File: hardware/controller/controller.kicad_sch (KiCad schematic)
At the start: 2 parts, among them U3 Baochip, U4 Baochip

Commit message: remove wrong part from controller board
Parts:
- removed U3, U4: Baochip, common:Dabao_Vendor_Substrate, symbol common:Dabao

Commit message: more controller board work
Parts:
- added U5, U6, U7, U8: ZX-PM2.54-1-16PY, easyeda2kicad:HDR-TH_16P-P2.54-V-F-1, symbol easyeda2kicad:ZX-PM2.54-1-16PY

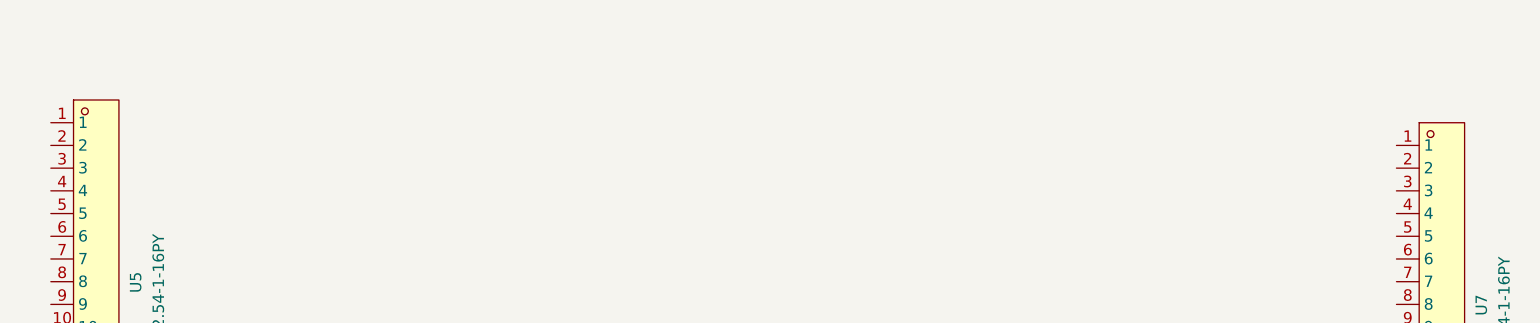
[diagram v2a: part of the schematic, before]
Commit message: adding labels and the barrel connector
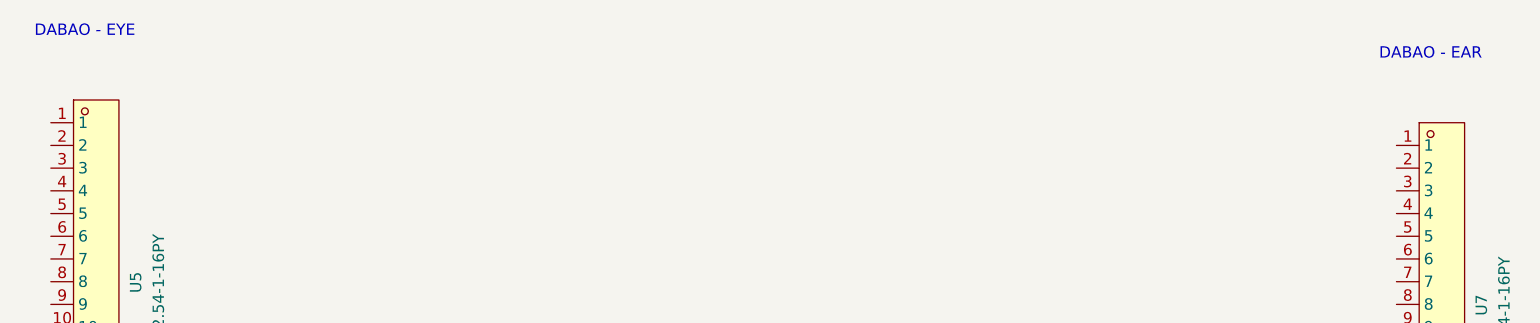
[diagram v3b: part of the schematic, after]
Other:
- note added: "DABAO - EAR"
- note added: "DABAO - EYE"
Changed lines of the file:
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@@
 	(generator_version "10.0")
 	(paper "A4")
+	(text "DABAO - EYE"
+		(exclude_from_sim no)
+		(at 97.79 27.94 0)
+		(effects
+			(font
+				(size 1.27 1.27)
+			)
+		)
+	)
+	(text "DABAO - EAR"
+		(exclude_from_sim no)
+		(at 248.285 30.48 0)
+		(effects
+			(font
+				(size 1.27 1.27)
+			)
+		)
+	)
 	(symbol
 		(lib_id "easyeda2kicad:ZX-PM2.54-1-16PY")

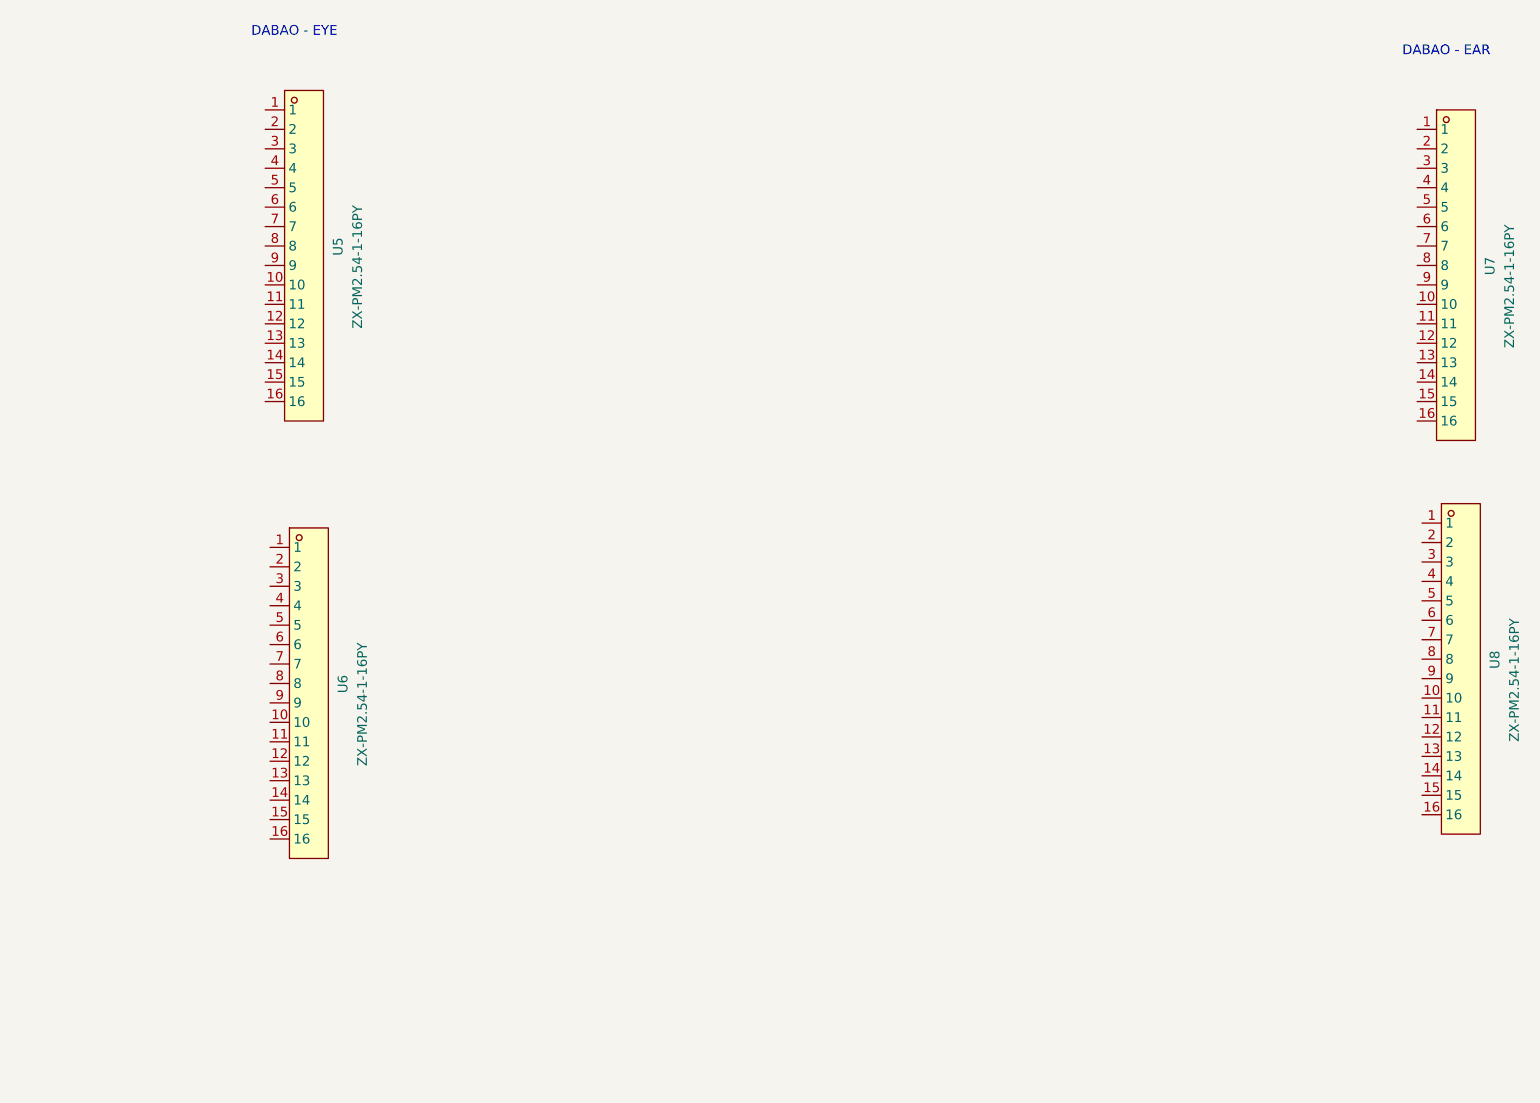
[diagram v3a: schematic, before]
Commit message: hook up all the dabao headers and one more voltage converter
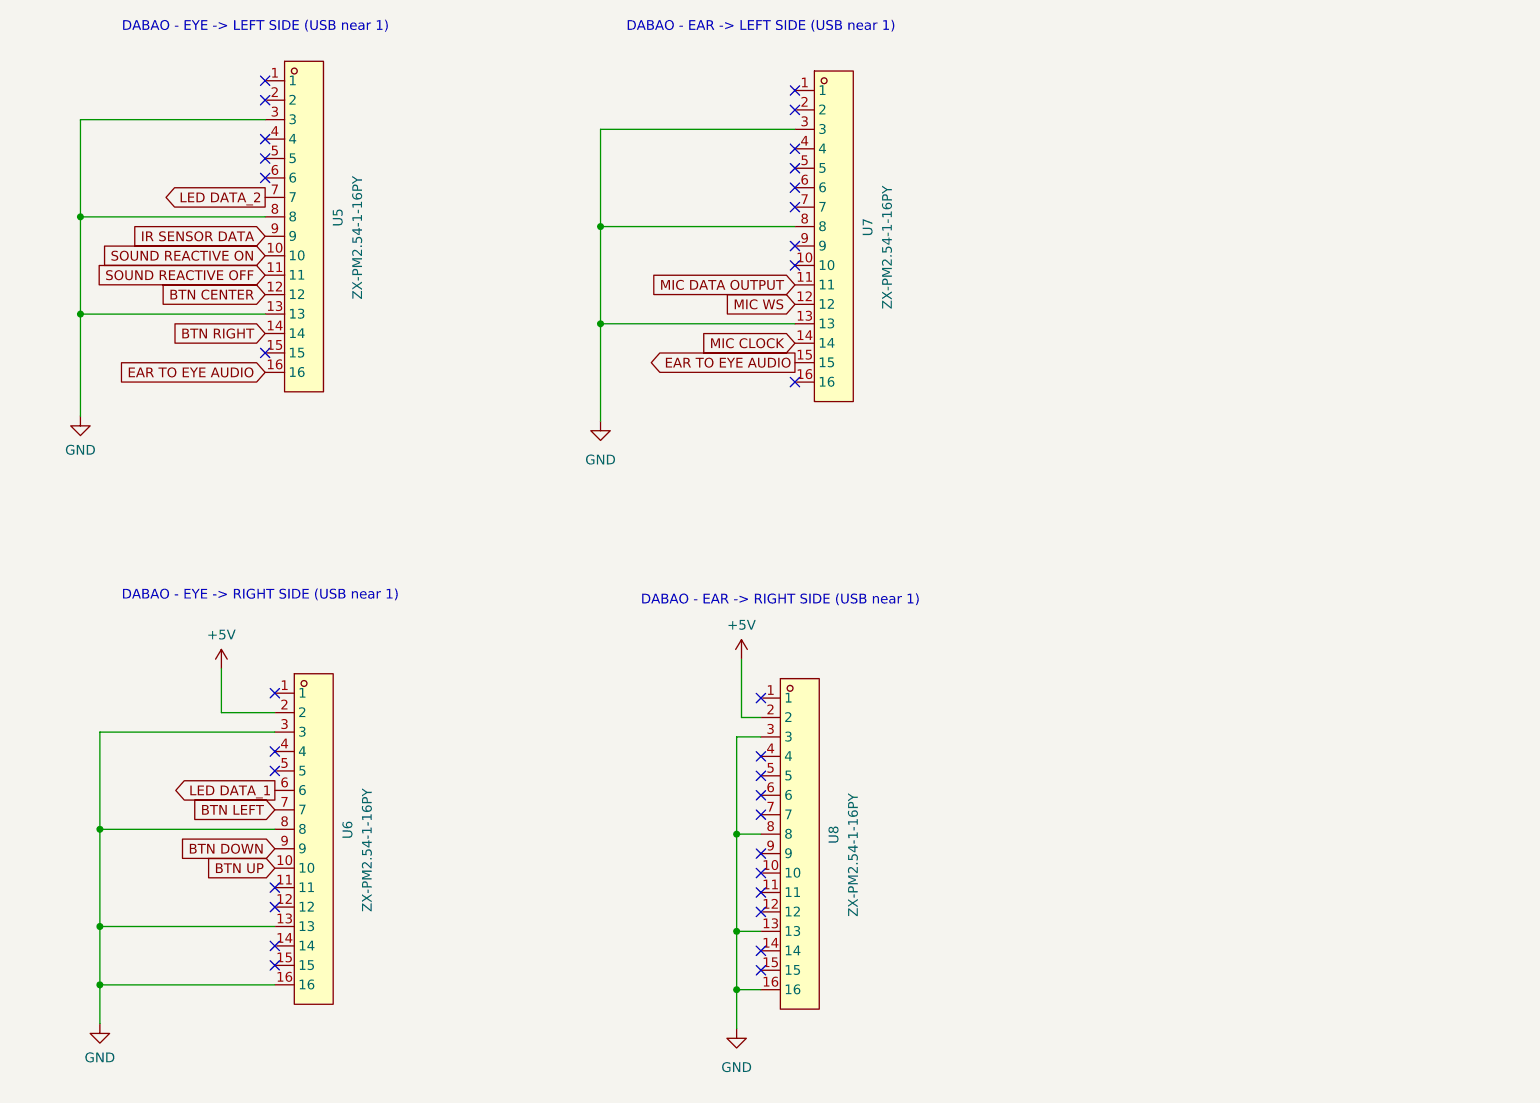
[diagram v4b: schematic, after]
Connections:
- net BTN UP: now reaches U6.10
- net GND: now reaches U6.13
- net GND: now also U5.13, U5.3, U5.8, U6.16, U6.3, U6.8, U7.13, U7.3, U7.8, U8.13, U8.16, U8.3, U8.8
- net +5V: now reaches U6.2
- net +5V: now also U8.2
- net LED DATA_1: now reaches U6.6
- net BTN LEFT: now reaches U6.7
- net BTN DOWN: now reaches U6.9
- net SOUND REACTIVE ON: now reaches U5.10
- net SOUND REACTIVE OFF: now reaches U5.11
- net BTN CENTER: now reaches U5.12
- net BTN RIGHT: now reaches U5.14
- net EAR TO EYE AUDIO: now reaches U5.16
- net EAR TO EYE AUDIO: now also U7.15
- net LED DATA_2: now reaches U5.7
- net IR SENSOR DATA: now reaches U5.9
- net MIC DATA OUTPUT: now reaches U7.11
- net MIC WS: now reaches U7.12
- net MIC CLOCK: now reaches U7.14
- no-connect marks 0 -> 33
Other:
- note added: "DABAO - EAR -> LEFT SIDE (USB near 1)"
- note added: "DABAO - EAR -> RIGHT SIDE (USB near 1)"
- note added: "DABAO - EYE -> LEFT SIDE (USB near 1)"
- note added: "DABAO - EYE -> RIGHT SIDE (USB near 1)"
- note removed: "DABAO - EAR"
- note removed: "DABAO - EYE"
- moved on the sheet: U5, U6, U7, U8

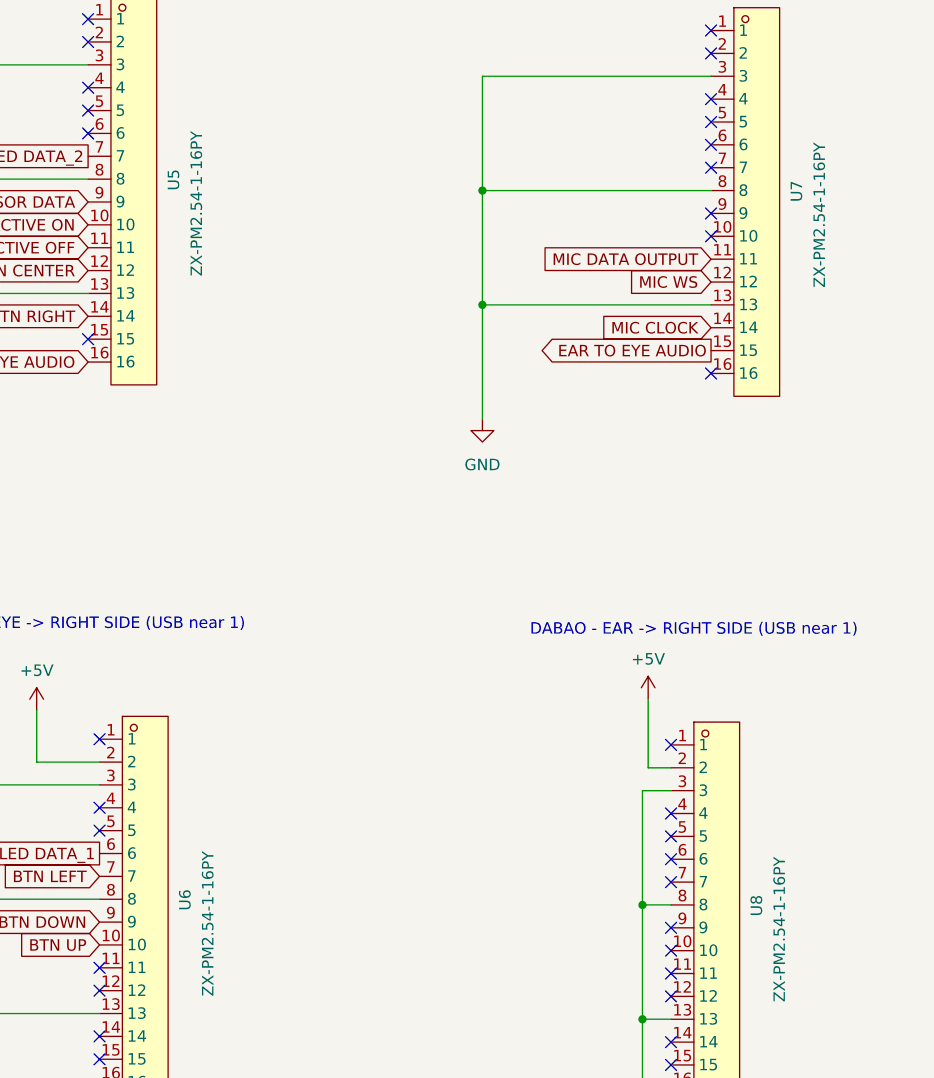
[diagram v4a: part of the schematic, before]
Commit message: re-order the numbers on the schematic for tidiness
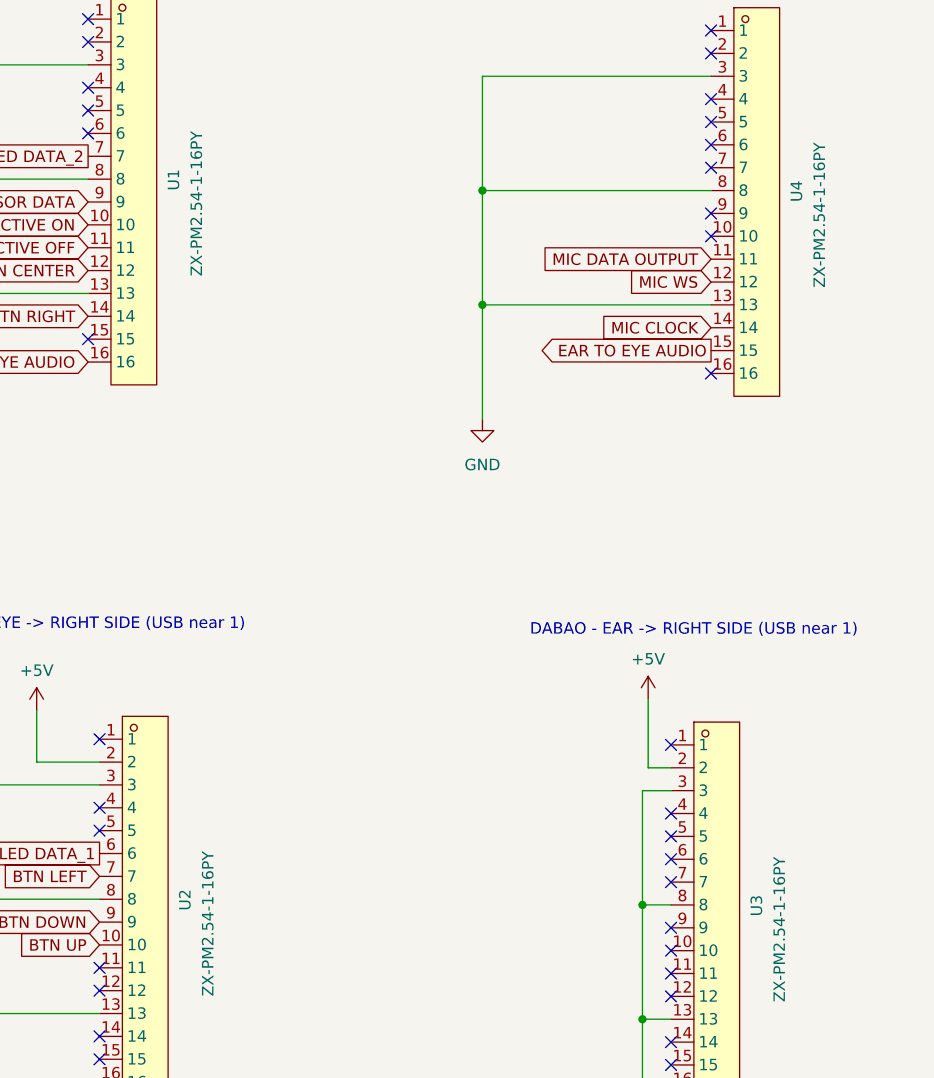
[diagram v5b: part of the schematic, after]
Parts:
- renumbered U5 to U1, U6 to U2, U8 to U3, U7 to U4
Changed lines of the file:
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@@
 		(dnp no)
 		(fields_autoplaced yes)
-		(property "Reference" "#PWR069"
+		(property "Reference" "#PWR06"
 			(at 156.21 113.665 0)
 			(hide yes)
@@
 			(project "controller"
 				(path "/2ec1a6cc-e255-4c8d-bf32-cfafd13c2b2e"
-					(reference "#PWR069")
+					(reference "#PWR06")
 					(unit 1)
 				)
@@
 		(in_pos_files yes)
 		(dnp no)
-		(property "Reference" "U6"
+		(property "Reference" "U2"
 			(at 104.775 133.35 90)
 			(show_name no)
@@
 			(project "controller"
 				(path "/2ec1a6cc-e255-4c8d-bf32-cfafd13c2b2e"
-					(reference "U6")
+					(reference "U2")
 					(unit 1)
 				)
@@
 		(dnp no)
 		(fields_autoplaced yes)
-		(property "Reference" "#PWR064"
+		(property "Reference" "#PWR01"
 			(at 69.85 84.455 0)
 			(hide yes)
@@
 			(project "controller"
 				(path "/2ec1a6cc-e255-4c8d-bf32-cfafd13c2b2e"
-					(reference "#PWR064")
+					(reference "#PWR01")
 					(unit 1)
 				)
@@
 		(dnp no)
 		(fields_autoplaced yes)
-		(property "Reference" "#PWR066"
+		(property "Reference" "#PWR02"
 			(at 72.39 163.83 0)
 			(hide yes)
@@
 			(project "controller"
 				(path "/2ec1a6cc-e255-4c8d-bf32-cfafd13c2b2e"
-					(reference "#PWR066")
+					(reference "#PWR02")
 					(unit 1)
 				)
@@
 		(in_pos_files yes)
 		(dnp no)
-		(property "Reference" "U8"
+		(property "Reference" "U3"
 			(at 168.275 133.985 90)
 			(show_name no)
@@
 			(project "controller"
 				(path "/2ec1a6cc-e255-4c8d-bf32-cfafd13c2b2e"
-					(reference "U8")
+					(reference "U3")
 					(unit 1)
 				)
@@
 		(dnp no)
 		(fields_autoplaced yes)
-		(property "Reference" "#PWR067"
+		(property "Reference" "#PWR04"
 			(at 137.795 85.09 0)
 			(hide yes)
@@
 			(project "controller"
 				(path "/2ec1a6cc-e255-4c8d-bf32-cfafd13c2b2e"
-					(reference "#PWR067")
+					(reference "#PWR04")
 					(unit 1)
 				)
@@
 		(dnp no)
 		(fields_autoplaced yes)
-		(property "Reference" "#PWR065"
+		(property "Reference" "#PWR03"
 			(at 88.265 114.935 0)
 			(hide yes)
@@
 			(project "controller"
 				(path "/2ec1a6cc-e255-4c8d-bf32-cfafd13c2b2e"
-					(reference "#PWR065")
+					(reference "#PWR03")
 					(unit 1)
 				)
@@
 		(in_pos_files yes)
 		(dnp no)
-		(property "Reference" "U5"
+		(property "Reference" "U1"
 			(at 103.505 53.34 90)
 			(show_name no)
@@
 			(project "controller"
 				(path "/2ec1a6cc-e255-4c8d-bf32-cfafd13c2b2e"
-					(reference "U5")
+					(reference "U1")
 					(unit 1)
 				)
@@
 		(dnp no)
 		(fields_autoplaced yes)
-		(property "Reference" "#PWR068"
+		(property "Reference" "#PWR05"
 			(at 155.575 164.465 0)
 			(hide yes)
@@
 			(project "controller"
 				(path "/2ec1a6cc-e255-4c8d-bf32-cfafd13c2b2e"
-					(reference "#PWR068")
+					(reference "#PWR05")
 					(unit 1)
 				)
@@
 		(in_pos_files yes)
 		(dnp no)
-		(property "Reference" "U7"
+		(property "Reference" "U4"
 			(at 172.72 54.61 90)
 			(show_name no)
@@
 			(project "controller"
 				(path "/2ec1a6cc-e255-4c8d-bf32-cfafd13c2b2e"
-					(reference "U7")
+					(reference "U4")
 					(unit 1)
 				)

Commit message: renaming parts for consistency
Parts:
- U1, U2, U3, U4: JLCPCB # C7499334 -> (none); LCSC Part # (none) -> C7499334
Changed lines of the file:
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@@
 			)
 		)
-		(property "JLCPCB #" "C7499334"
+		(property "LCSC Part #" "C7499334"
 			(at 99.06 170.18 0)
 			(hide yes)
@@
 			)
 		)
-		(property "JLCPCB #" "C7499334"
+		(property "LCSC Part #" "C7499334"
 			(at 162.56 170.815 0)
 			(hide yes)
@@
 			)
 		)
-		(property "JLCPCB #" "C7499334"
+		(property "LCSC Part #" "C7499334"
 			(at 97.79 90.17 0)
 			(hide yes)
@@
 			)
 		)
-		(property "JLCPCB #" "C7499334"
+		(property "LCSC Part #" "C7499334"
 			(at 167.005 91.44 0)
 			(hide yes)

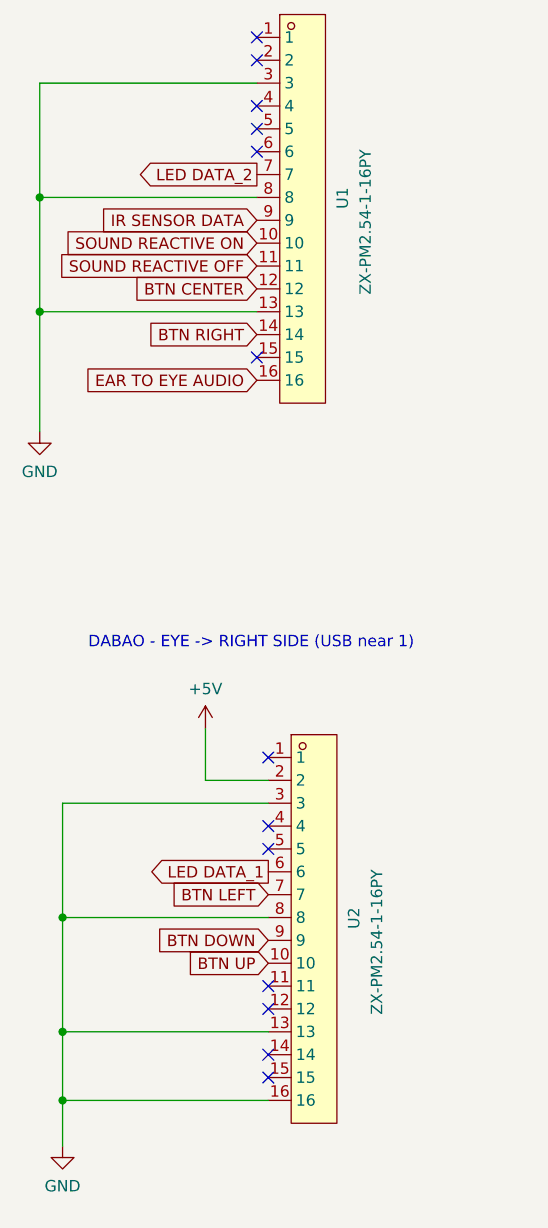
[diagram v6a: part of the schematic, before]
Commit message: rearrange the pins a bit and less insane routing
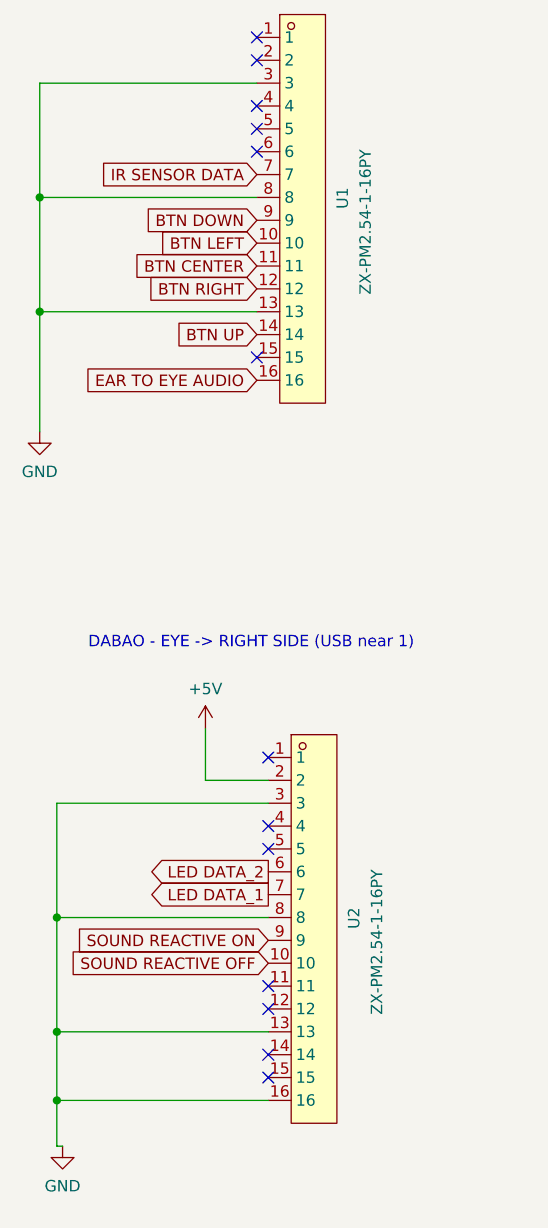
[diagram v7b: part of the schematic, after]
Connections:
- net BTN CENTER: now also U1.11; no longer U1.12
- net BTN DOWN: now also U1.9; no longer U2.9
- net BTN LEFT: now also U1.10; no longer U2.7
- net BTN RIGHT: now also U1.12; no longer U1.14
- net BTN UP: now also U1.14; no longer U2.10
- net IR SENSOR DATA: now also U1.7; no longer U1.9
- net LED DATA_1: now also U2.7; no longer U2.6
- net LED DATA_2: now also U2.6; no longer U1.7
- net SOUND REACTIVE OFF: now also U2.10; no longer U1.11
- net SOUND REACTIVE ON: now also U2.9; no longer U1.10

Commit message: controller layout updates
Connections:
- net +5V: now also U4.2; no longer U3.2
- net EAR TO EYE AUDIO: now also U3.15; no longer U4.15
- net GND: now also U4.16; no longer U3.16
- net MIC CLOCK: now also U4.12; no longer U4.14
- net MIC DATA OUTPUT: now also U4.10; no longer U4.11
- net MIC WS: now also U4.9; no longer U4.12
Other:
- moved on the sheet: U3, U4
